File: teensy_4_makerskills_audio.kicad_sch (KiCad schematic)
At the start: 11 parts, among them J1 Teensy, J2 Teensy, J3 Output, J4 minijack, U1 PT8211, U2 INMP441

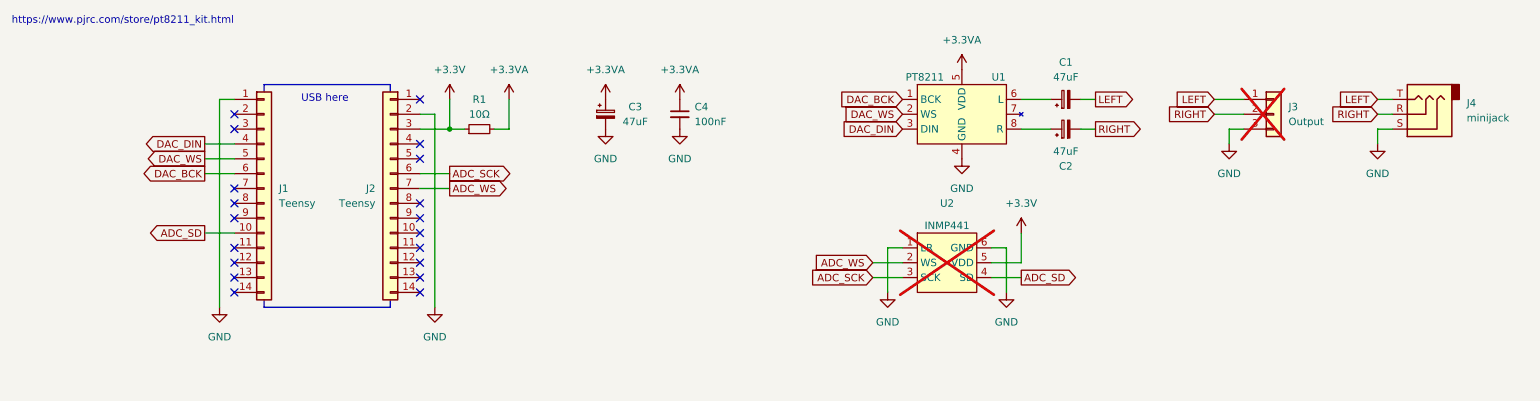
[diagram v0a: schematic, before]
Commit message: Pin usage marked, PCBA teensy pins, mic smd sockets
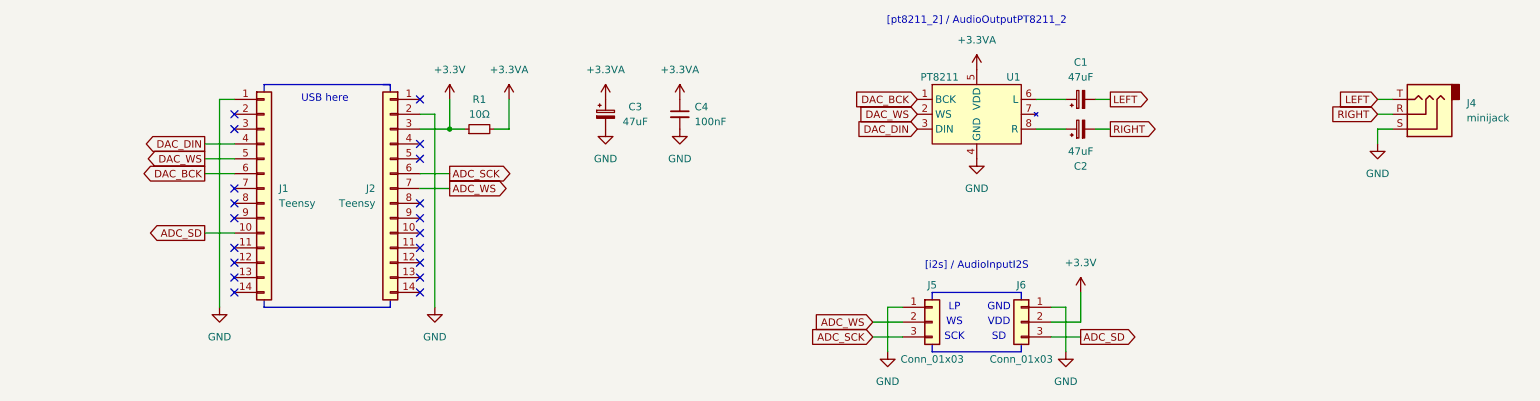
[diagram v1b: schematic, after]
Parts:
- removed J3: Output, Connector_PinHeader_2.54mm:PinHeader_1x03_P2.54mm_Vertical, symbol Connector_Generic:Conn_01x03
- removed U2: INMP441, teensy:INMP441, symbol Teensy-audio:INMP441-board
- added J5, J6: Conn_01x03, Connector_PinSocket_2.54mm:PinSocket_1x03_P2.54mm_Vertical_SMD_Pin1Left, symbol Connector_Generic:Conn_01x03
- J1, J2: FT Rotation Offset (none) -> 90; LCSC - -> C2894937
- J4: FT Position Offset (none) -> 0,1; FT Rotation Offset (none) -> 90; JLCPCB Position Offset -0.02,1.8 -> (none); JLCPCB Rotation Offset 90 -> (none)
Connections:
- net +3.3V: now also J6.2 (Pin_2)
- net ADC_SCK: now also J5.3 (Pin_3)
- net ADC_SD: now also J6.3 (Pin_3)
- net ADC_WS: now also J5.2 (Pin_2)
- net GND: now also J5.1 (Pin_1), J6.1 (Pin_1)
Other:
- note added: "GND"
- note added: "LP"
- note added: "SCK"
- note added: "SD"
- note added: "VDD"
- note added: "WS"
- note added: "[i2s] / AudioInputI2S"
- note added: "[pt8211_2] / AudioOutputPT8211_2"
- note removed: "https://www.pjrc.com/store/pt8211_kit.html"
- title: Audio-in-uit-bord -> Teensy 4 maker skills mic+dac
- moved on the sheet: C1, C2, U1
